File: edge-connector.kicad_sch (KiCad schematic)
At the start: 25 parts, among them J9 dc-scm-rev-1-0-edge-connector

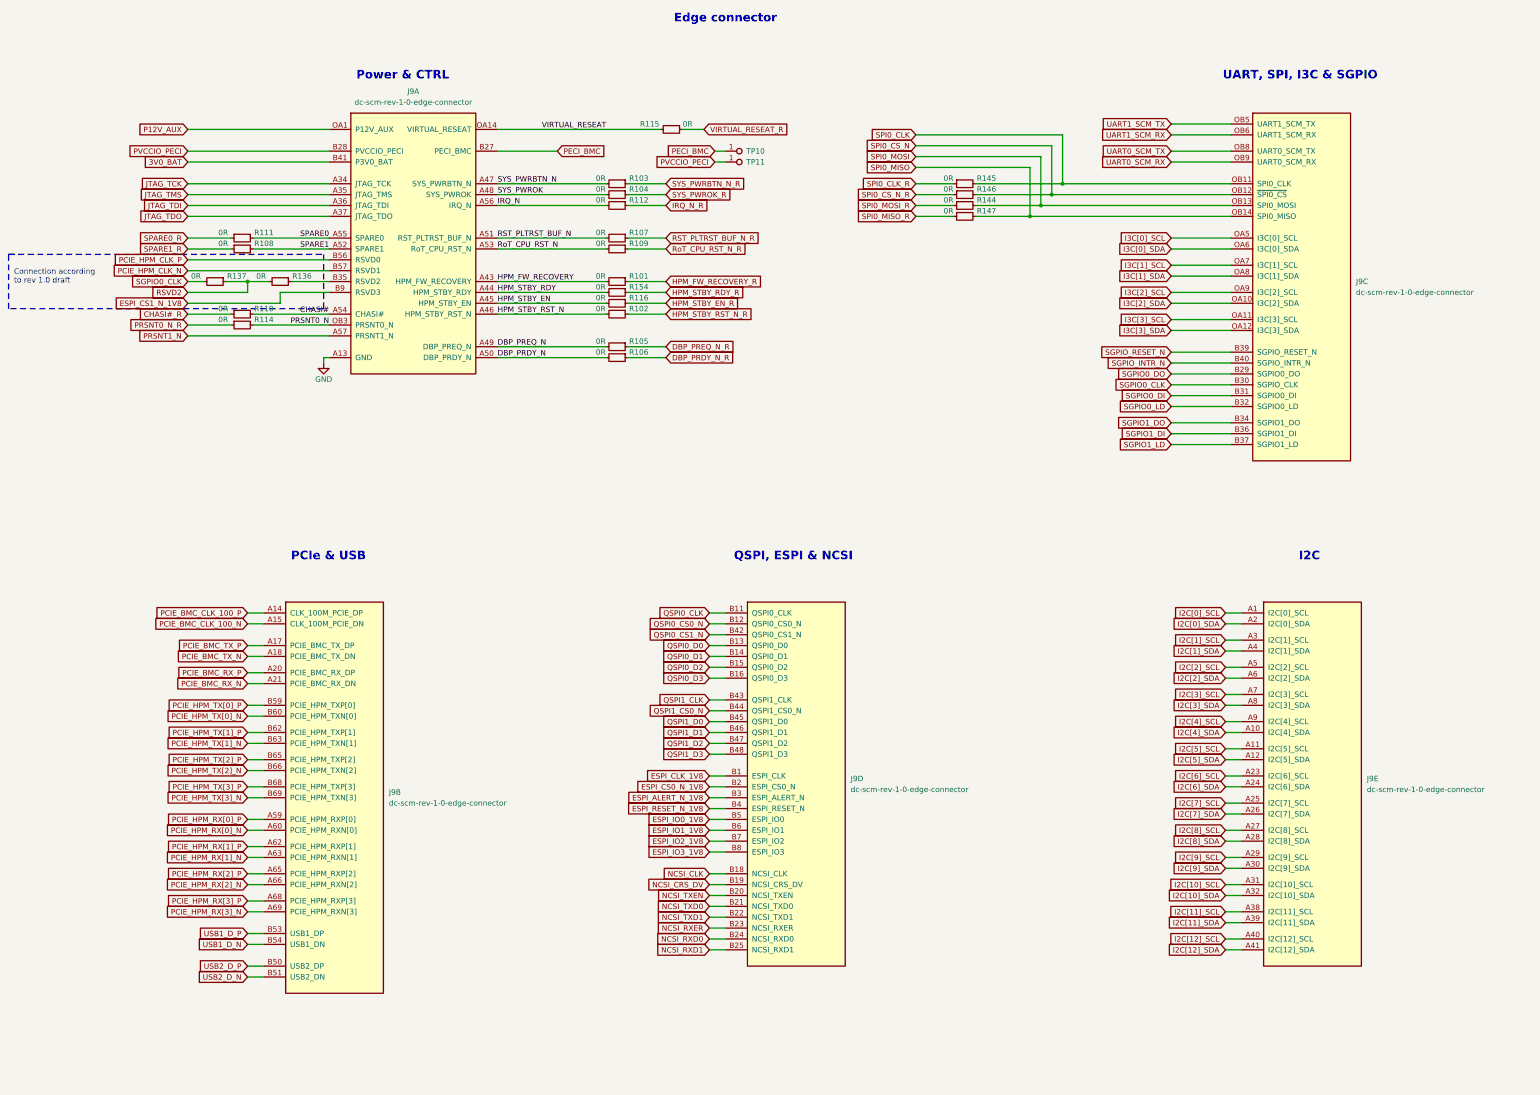
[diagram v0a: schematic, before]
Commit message: [#68236] Update symbols and footprints, clean ERC and DRC
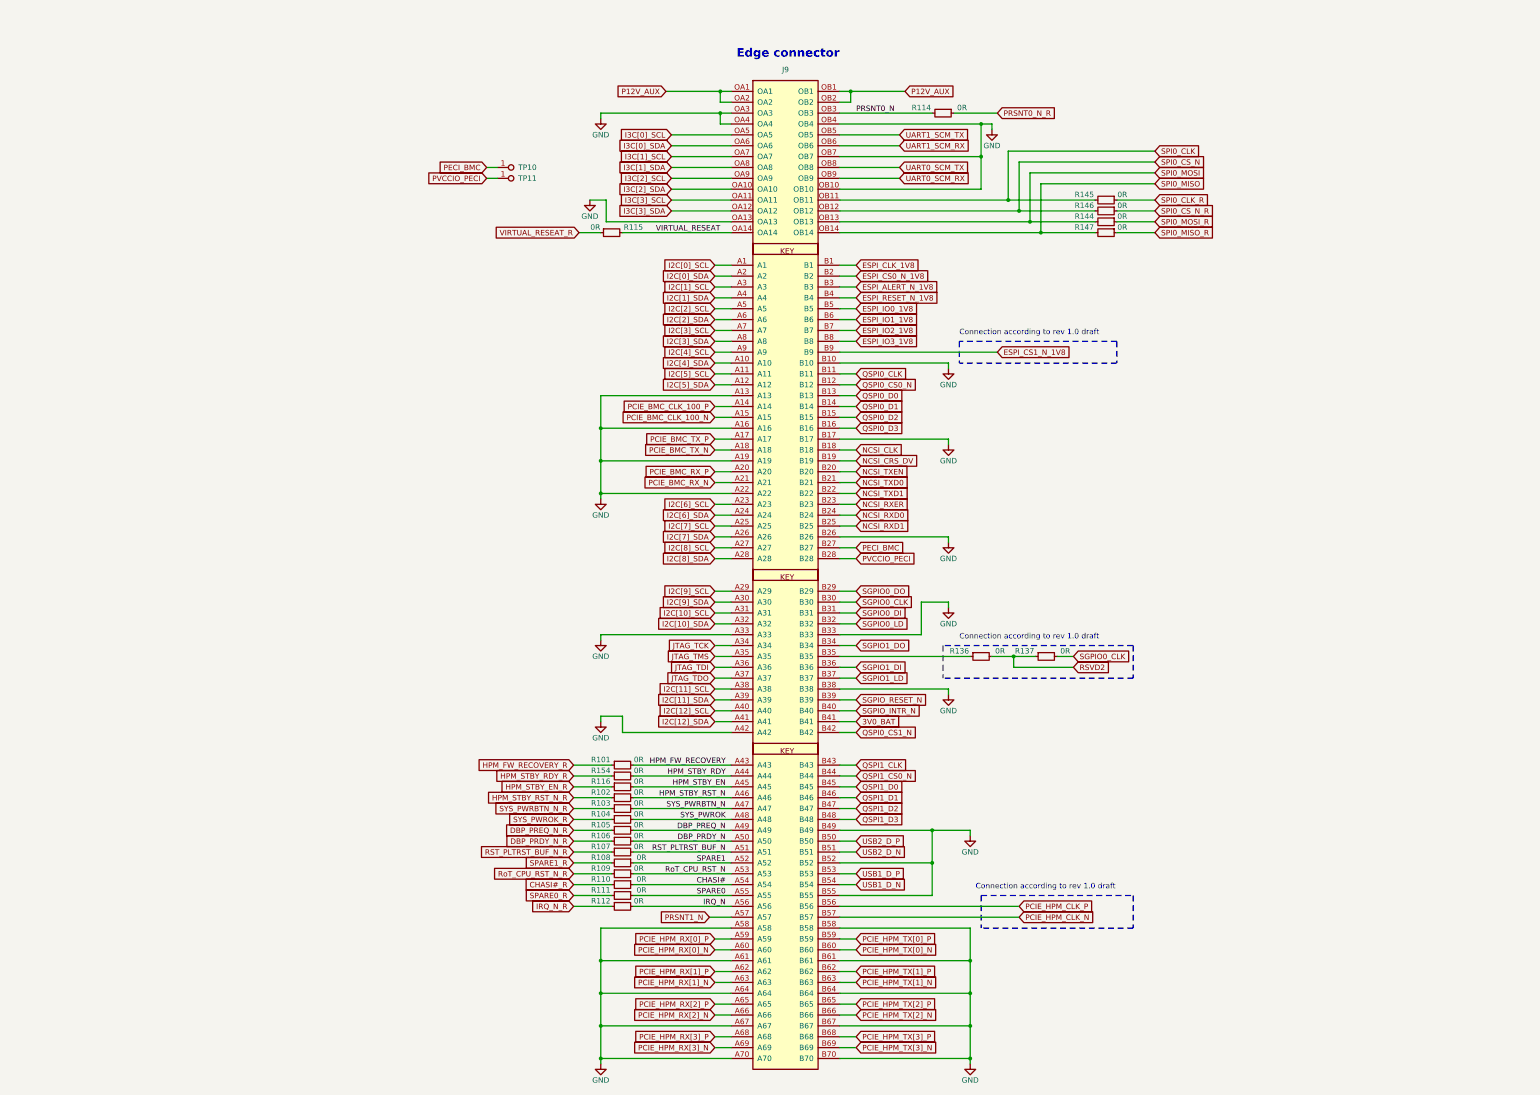
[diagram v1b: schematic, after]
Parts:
- removed J9: dc-scm-rev-1-0-edge-connector, antmicro-footprints:SFF-TA-1002-4C+-rev-1-0-0, symbol antmicroPciConnectors:dc-scm-rev-1-0-edge-connector
- added J9: SFF-TA-1002-4C+, antmicro-footprints:SFF-TA-1002-4C+, symbol antmicroPciConnectors:SFF-TA-1002-4C+
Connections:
- net 3V0_BAT: now also J9.B41
- net CHASI#: now also R110.1, J9.A54; no longer R110.2
- net CHASI#_R: now also R110.2; no longer R110.1
- net DBP_PRDY_N: now also J9.A50
- net DBP_PREQ_N: now also J9.A49
- net ESPI_ALERT_N_1V8: now also J9.B3
- net ESPI_CLK_1V8: now also J9.B1
- net ESPI_CS0_N_1V8: now also J9.B2
- net ESPI_CS1_N_1V8: now also J9.B9
- net ESPI_IO0_1V8: now also J9.B5
- net ESPI_IO1_1V8: now also J9.B6
- net ESPI_IO2_1V8: now also J9.B7
- net ESPI_IO3_1V8: now also J9.B8
- net ESPI_RESET_N_1V8: now also J9.B4
- net GND: now also J9.A13, J9.A16, J9.A19, J9.A22, J9.A33, J9.A42, J9.A58, J9.A61, J9.A64, J9.A67, J9.A70, J9.B10, J9.B17, J9.B26, J9.B33, J9.B38, J9.B49, J9.B52, J9.B55, J9.B58, J9.B61, J9.B64, J9.B67, J9.B70, J9.OA13, J9.OA3, J9.OA4, J9.OB10, J9.OB4, J9.OB7
- net HPM_FW_RECOVERY: now also J9.A43
- net HPM_STBY_EN: now also J9.A45
- net HPM_STBY_RDY: now also J9.A44
- net HPM_STBY_RST_N: now also J9.A46
- net I2C[0]_SCL: now also J9.A1
- net I2C[0]_SDA: now also J9.A2
- net I2C[10]_SCL: now also J9.A31
- net I2C[10]_SDA: now also J9.A32
- net I2C[11]_SCL: now also J9.A38
- net I2C[11]_SDA: now also J9.A39
- net I2C[12]_SCL: now also J9.A40
- net I2C[12]_SDA: now also J9.A41
- net I2C[1]_SCL: now also J9.A3
- net I2C[1]_SDA: now also J9.A4
- net I2C[2]_SCL: now also J9.A5
- net I2C[2]_SDA: now also J9.A6
- net I2C[3]_SCL: now also J9.A7
- net I2C[3]_SDA: now also J9.A8
- net I2C[4]_SCL: now also J9.A9
- net I2C[4]_SDA: now also J9.A10
- net I2C[5]_SCL: now also J9.A11
- net I2C[5]_SDA: now also J9.A12
- net I2C[6]_SCL: now also J9.A23
- net I2C[6]_SDA: now also J9.A24
- net I2C[7]_SCL: now also J9.A25
- net I2C[7]_SDA: now also J9.A26
- net I2C[8]_SCL: now also J9.A27
- net I2C[8]_SDA: now also J9.A28
- net I2C[9]_SCL: now also J9.A29
- net I2C[9]_SDA: now also J9.A30
- net I3C[0]_SCL: now also J9.OA5
- net I3C[0]_SDA: now also J9.OA6
- net I3C[1]_SCL: now also J9.OA7
- net I3C[1]_SDA: now also J9.OA8
- net I3C[2]_SCL: now also J9.OA9
- net I3C[2]_SDA: now also J9.OA10
- net I3C[3]_SCL: now also J9.OA11
- net I3C[3]_SDA: now also J9.OA12
- net IRQ_N: now also J9.A56
- net JTAG_TCK: now also J9.A34
- net JTAG_TDI: now also J9.A36
- net JTAG_TDO: now also J9.A37
- net JTAG_TMS: now also J9.A35
- net NCSI_CLK: now also J9.B18
- net NCSI_CRS_DV: now also J9.B19
- net NCSI_RXD0: now also J9.B24
- net NCSI_RXD1: now also J9.B25
- net NCSI_RXER: now also J9.B23
- net NCSI_TXD0: now also J9.B21
- net NCSI_TXD1: now also J9.B22
- net NCSI_TXEN: now also J9.B20
- net P12V_AUX: now also J9.OA1, J9.OA2, J9.OB1, J9.OB2
- net PCIE_BMC_CLK_100_N: now also J9.A15
- net PCIE_BMC_CLK_100_P: now also J9.A14
- net PCIE_BMC_RX_N: now also J9.A21
- net PCIE_BMC_RX_P: now also J9.A20
- net PCIE_BMC_TX_N: now also J9.A18
- net PCIE_BMC_TX_P: now also J9.A17
- net PCIE_HPM_CLK_N: now also J9.B57
- net PCIE_HPM_CLK_P: now also J9.B56
- net PCIE_HPM_RX[0]_N: now also J9.A60
- net PCIE_HPM_RX[0]_P: now also J9.A59
- net PCIE_HPM_RX[1]_N: now also J9.A63
- net PCIE_HPM_RX[1]_P: now also J9.A62
- net PCIE_HPM_RX[2]_N: now also J9.A66
- net PCIE_HPM_RX[2]_P: now also J9.A65
- net PCIE_HPM_RX[3]_N: now also J9.A69
- net PCIE_HPM_RX[3]_P: now also J9.A68
- net PCIE_HPM_TX[0]_N: now also J9.B60
- net PCIE_HPM_TX[0]_P: now also J9.B59
- net PCIE_HPM_TX[1]_N: now also J9.B63
- net PCIE_HPM_TX[1]_P: now also J9.B62
- net PCIE_HPM_TX[2]_N: now also J9.B66
- net PCIE_HPM_TX[2]_P: now also J9.B65
- net PCIE_HPM_TX[3]_N: now also J9.B69
- net PCIE_HPM_TX[3]_P: now also J9.B68
- net PECI_BMC: now also J9.B27
- net PRSNT0_N: now also J9.OB3
- net PRSNT1_N: now also J9.A57
- net PVCCIO_PECI: now also J9.B28
- net QSPI0_CLK: now also J9.B11
- net QSPI0_CS0_N: now also J9.B12
- net QSPI0_CS1_N: now also J9.B42
- net QSPI0_D0: now also J9.B13
- net QSPI0_D1: now also J9.B14
- net QSPI0_D2: now also J9.B15
- net QSPI0_D3: now also J9.B16
- net QSPI1_CLK: now also J9.B43
- net QSPI1_CS0_N: now also J9.B44
- net QSPI1_D0: now also J9.B45
- net QSPI1_D1: now also J9.B46
- net QSPI1_D2: now also J9.B47
- net QSPI1_D3: now also J9.B48
- net RST_PLTRST_BUF_N: now also J9.A51
- net RoT_CPU_RST_N: now also J9.A53
- net SGPIO0_CLK: now also J9.B30
- net SGPIO0_DI: now also J9.B31
- net SGPIO0_DO: now also J9.B29
- net SGPIO0_LD: now also J9.B32
- net SGPIO1_DI: now also J9.B36
- net SGPIO1_DO: now also J9.B34
- net SGPIO1_LD: now also J9.B37
- net SGPIO_INTR_N: now also J9.B40
- net SGPIO_RESET_N: now also J9.B39
- net SPARE0: now also R111.1, J9.A55; no longer R111.2
- net SPARE0_R: now also R111.2; no longer R111.1
- net SPARE1: now also R108.1, J9.A52; no longer R108.2
- net SPARE1_R: now also R108.2; no longer R108.1
- net SPI0_CLK: now also J9.OB11
- net SPI0_CS_N: now also J9.OB12
- net SPI0_MISO: now also J9.OB14
- net SPI0_MOSI: now also J9.OB13
- net SYS_PWRBTN_N: now also J9.A47
- net SYS_PWROK: now also J9.A48
- net UART0_SCM_RX: now also J9.OB9
- net UART0_SCM_TX: now also J9.OB8
- net UART1_SCM_RX: now also J9.OB6
- net UART1_SCM_TX: now also J9.OB5
- net USB1_D_N: now also J9.B54
- net USB1_D_P: now also J9.B53
- net USB2_D_N: now also J9.B51
- net USB2_D_P: now also J9.B50
- net VIRTUAL_RESEAT: now also J9.OA14
- net at R136.1: now also J9.B35
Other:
- note removed: "I2C"
- note removed: "PCIe & USB"
- note removed: "Power & CTRL"
- note removed: "QSPI, ESPI & NCSI"
- note removed: "UART, SPI, I3C & SGPIO"
- moved on the sheet: R101, R102, R103, R104, R105, R106, R107, R114, R115, R116, R136, R137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

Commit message: bom changes
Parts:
- R101, R102, R103, R104, R105, R106, R107, R108, R109, R110, R111, R112, R114, R115, R116, R136, R137, R144, R145, R146, R147, R154: MPN ERJ2GE0R00X -> RC0402JR-7D0RL; Manufacturer Panasonic -> YAGEO

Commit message: "In the process of upgrading the ddr memory"
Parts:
- removed J9: SFF-TA-1002-4C+, antmicro-footprints:SFF-TA-1002-4C+, symbol antmicroPciConnectors:SFF-TA-1002-4C+
